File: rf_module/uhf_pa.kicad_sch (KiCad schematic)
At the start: 28 parts, among them U8 FPF2701, U9 TQP7M9106

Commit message: feat: minor schematic adjustments and pcb layout
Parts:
- removed NT1: Net-Tie_2, NetTie:NetTie-2_SMD_Pad0.5mm, symbol Device:NetTie_2
- removed R11: 0, Resistor_SMD:R_0603_1608Metric, symbol Device:R_Small
- TP4: value PA_FAULT -> PA_Fault; footprint lsf-kicad-lib:TestPoint_D0.8mm_Mask-Only -> TestPoint:TestPoint_Pad_D1.0mm
- TP5: footprint lsf-kicad-lib:TestPoint_D0.8mm_Mask-Only -> TestPoint:TestPoint_Pad_D1.0mm
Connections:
- net GND: now also U8.2 (PGOOD)
- net at C36.1, U9.1 (VBIAS): now also R10.1
- net 5V_TX_Filt: now reaches C43.2, FB1.1, L17.1
- net RF_Amp_Match2: now reaches C45.1, L19.2
- net RF_Amp_Out: now reaches C44.1, L17.2, U9.14 (RFOUT/VCC), U9.15 (RFOUT/VCC), U9.16 (RFOUT/VCC)
- net RF_Amp_Match1: now reaches C44.2, L18.1, L19.1
- net RF_Amp_In: now reaches L16.2, U9.4 (RFIN), U9.5 (RFIN)
- net PA_FAULT renamed PA_Fault
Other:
- moved on the sheet: C45

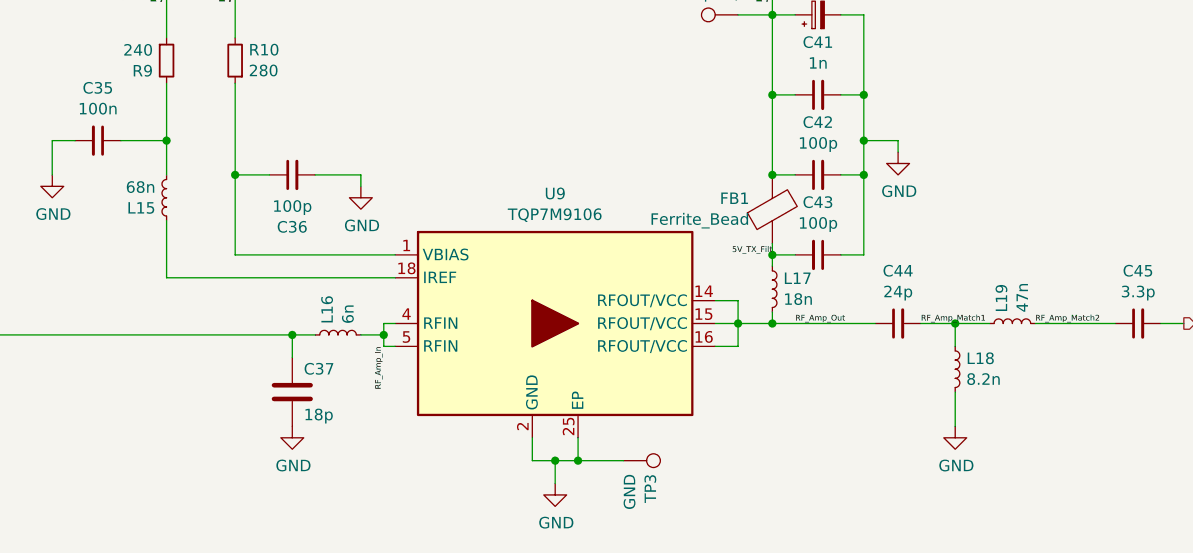
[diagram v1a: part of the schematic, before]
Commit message: feat: implement LNA activation on RX and PA_Enable in schematic (layout TODO)
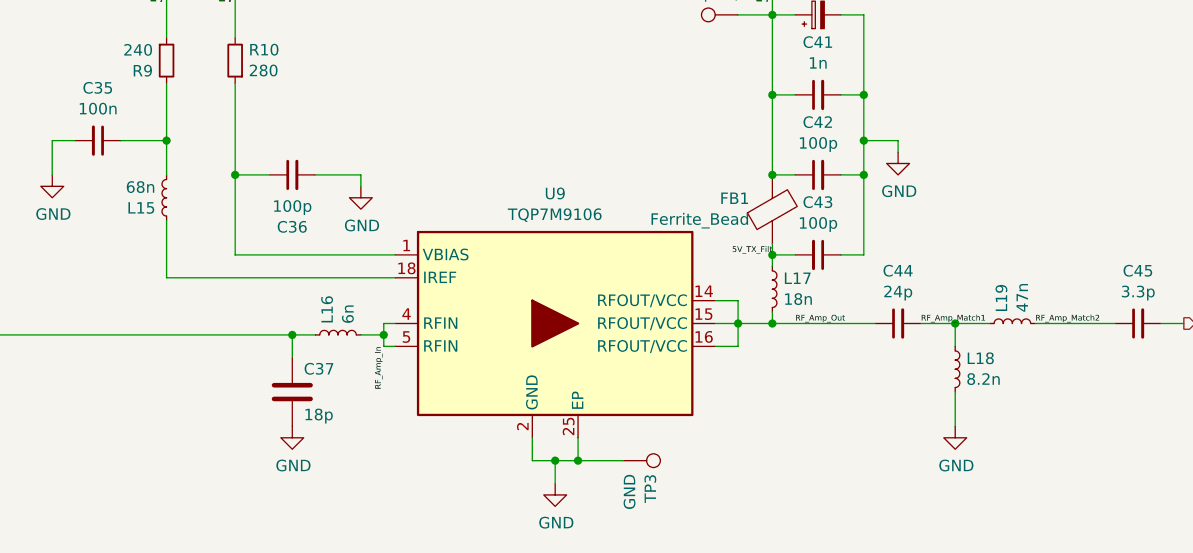
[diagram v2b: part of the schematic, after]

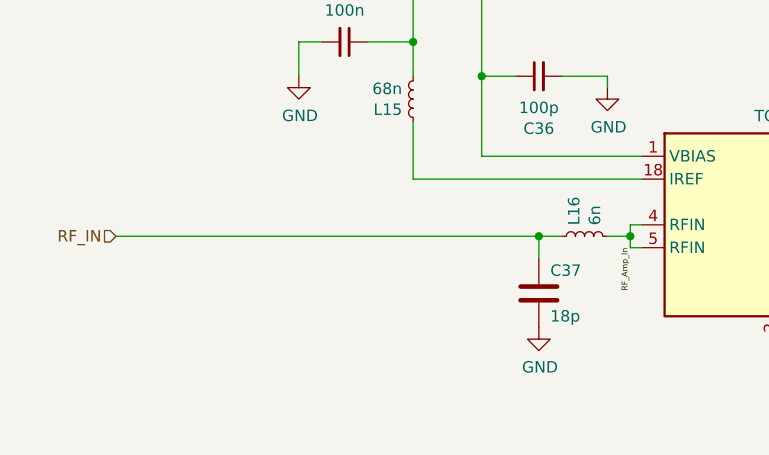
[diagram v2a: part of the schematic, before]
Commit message: fix: component values of TX PA input matching and filter
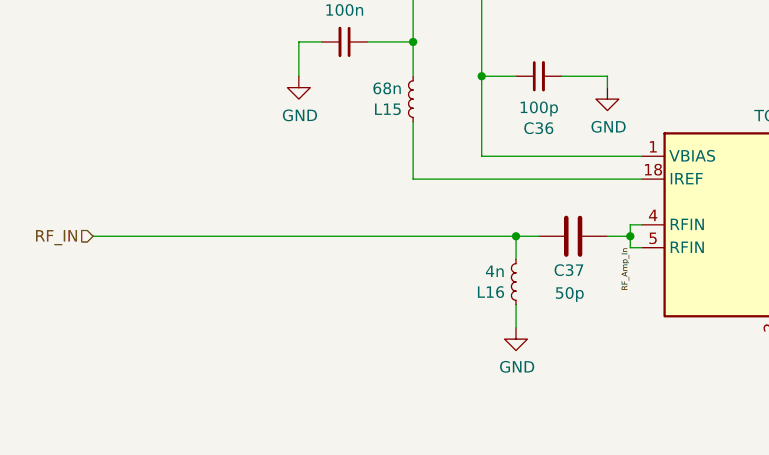
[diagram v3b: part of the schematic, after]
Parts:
- C37: value 18p -> 50p
- L16: value 6n -> 4n
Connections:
- net GND: now also L16.1; no longer C37.2
- net RF_Amp_In: now also C37.2; no longer L16.2
- net RF_IN: now also L16.2; no longer L16.1
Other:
- moved on the sheet: C37, L16
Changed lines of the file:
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@@
   (junction (at 147.32 146.05) (diameter 0) (color 0 0 0 0)
   )
-  (junction (at 118.11 132.08) (diameter 0) (color 0 0 0 0)
+  (junction (at 115.57 132.08) (diameter 0) (color 0 0 0 0)
   )
   (junction (at 167.64 130.81) (diameter 0) (color 0 0 0 0)
@@
     (stroke (width 0) (type default))
   )
-  (wire (pts (xy 71.12 132.08) (xy 118.11 132.08))
+  (wire (pts (xy 68.58 132.08) (xy 115.57 132.08))
     (stroke (width 0) (type default))
   )
@@
     (stroke (width 0) (type default))
   )
+  (wire (pts (xy 115.57 139.7) (xy 115.57 142.24))
+    (stroke (width 0) (type default))
+  )
   (wire (pts (xy 104.14 110.49) (xy 104.14 114.3))
     (stroke (width 0) (type default))
@@
     (stroke (width 0) (type default))
   )
-  (wire (pts (xy 120.65 132.08) (xy 118.11 132.08))
+  (wire (pts (xy 118.11 132.08) (xy 115.57 132.08))
     (stroke (width 0) (type default))
   )
@@
     (stroke (width 0) (type default))
   )
-  (wire (pts (xy 118.11 132.08) (xy 118.11 134.62))
+  (wire (pts (xy 115.57 132.08) (xy 115.57 134.62))
     (stroke (width 0) (type default))
   )
@@
     (effects (font (size 0.635 0.635)) (justify right bottom))
   )
-  (hierarchical_label "RF_IN" (shape input) (at 71.12 132.08 180) (fields_autoplaced)
+  (hierarchical_label "RF_IN" (shape input) (at 68.58 132.08 180) (fields_autoplaced)
     (effects (font (size 1.27 1.27)) (justify right))
   )
@@
     )
   )
-  (symbol (lib_name "GND_4") (lib_id "power:GND") (at 118.11 142.24 0) (unit 1)
-    (in_bom yes) (on_board yes) (dnp no)
-    (property "Reference" "#PWR?" (at 118.11 148.59 0)
-      (effects (font (size 1.27 1.27)) hide)
-    )
-    (property "Value" "GND" (at 118.237 146.6342 0)
-      (effects (font (size 1.27 1.27)))
-    )
-    (property "Footprint" "" (at 118.11 142.24 0)
-      (effects (font (size 1.27 1.27)) hide)
-    )
-    (property "Datasheet" "" (at 118.11 142.24 0)
+  (symbol (lib_name "GND_4") (lib_id "power:GND") (at 115.57 142.24 0) (unit 1)
+    (in_bom yes) (on_board yes) (dnp no)
+    (property "Reference" "#PWR?" (at 115.57 148.59 0)
+      (effects (font (size 1.27 1.27)) hide)
+    )
+    (property "Value" "GND" (at 115.697 146.6342 0)
+      (effects (font (size 1.27 1.27)))
+    )
+    (property "Footprint" "" (at 115.57 142.24 0)
+      (effects (font (size 1.27 1.27)) hide)
+    )
+    (property "Datasheet" "" (at 115.57 142.24 0)
       (effects (font (size 1.27 1.27)) hide)
     )
@@
     )
   )
-  (symbol (lib_id "Device:L_Small") (at 123.19 132.08 90) (unit 1)
-    (in_bom yes) (on_board yes) (dnp no)
-    (property "Reference" "L16" (at 122.0216 130.8608 0)
+  (symbol (lib_id "Device:L_Small") (at 115.57 137.16 180) (unit 1)
+    (in_bom yes) (on_board yes) (dnp no)
+    (property "Reference" "L16" (at 114.3508 138.3284 0)
       (effects (font (size 1.27 1.27)) (justify left))
     )
-    (property "Value" "6n" (at 124.333 130.8608 0)
+    (property "Value" "4n" (at 114.3508 136.017 0)
       (effects (font (size 1.27 1.27)) (justify left))
     )
-    (property "Footprint" "Inductor_SMD:L_0402_1005Metric" (at 123.19 132.08 0)
-      (effects (font (size 1.27 1.27)) hide)
-    )
-    (property "Datasheet" "~" (at 123.19 132.08 0)
-      (effects (font (size 1.27 1.27)) hide)
-    )
-    (property "Mnf." "TDK" (at 123.19 132.08 0)
-      (effects (font (size 1.27 1.27)) hide)
-    )
-    (property "PartNumber" "MHQ1005P68NGTD25" (at 123.19 132.08 0)
+    (property "Footprint" "Inductor_SMD:L_0402_1005Metric" (at 115.57 137.16 0)
+      (effects (font (size 1.27 1.27)) hide)
+    )
+    (property "Datasheet" "~" (at 115.57 137.16 0)
+      (effects (font (size 1.27 1.27)) hide)
+    )
+    (property "Mnf." "TDK" (at 115.57 137.16 0)
+      (effects (font (size 1.27 1.27)) hide)
+    )
+    (property "PartNumber" "MHQ1005P68NGTD25" (at 115.57 137.16 0)
       (effects (font (size 1.27 1.27)) hide)
     )
@@
     )
   )
-  (symbol (lib_id "Device:C") (at 118.11 138.43 0) (unit 1)
-    (in_bom yes) (on_board yes) (dnp no)
-    (property "Reference" "C37" (at 119.38 135.89 0)
+  (symbol (lib_id "Device:C") (at 121.92 132.08 90) (unit 1)
+    (in_bom yes) (on_board yes) (dnp no)
+    (property "Reference" "C37" (at 123.19 135.89 90)
       (effects (font (size 1.27 1.27)) (justify left))
     )
-    (property "Value" "18p" (at 119.38 140.97 0)
+    (property "Value" "50p" (at 123.19 138.43 90)
       (effects (font (size 1.27 1.27)) (justify left))
     )
-    (property "Footprint" "Capacitor_SMD:C_0402_1005Metric" (at 119.0752 142.24 0)
-      (effects (font (size 1.27 1.27)) hide)
-    )
-    (property "Datasheet" "~" (at 118.11 138.43 0)
-      (effects (font (size 1.27 1.27)) hide)
-    )
+    (property "Footprint" "Capacitor_SMD:C_0402_1005Metric" (at 125.73 131.1148 0)
+      (effects (font (size 1.27 1.27)) hide)
+    )
+    (property "Datasheet" "~" (at 121.92 132.08 0)
+      (effects (font (size 1.27 1.27)) hide)
+    )
